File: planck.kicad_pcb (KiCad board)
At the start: 4 copper layers, 38.8 x 39.8 mm, 32 parts, among them J1 USB_C_Receptacle_USB2.0, K1 KEYSW, K2 KEYSW, K3 KEYSW, K4 KEYSW, SW1 SW_PUSH, U1 ATmega32U4-M, Y1 Crystal_GND24_Small

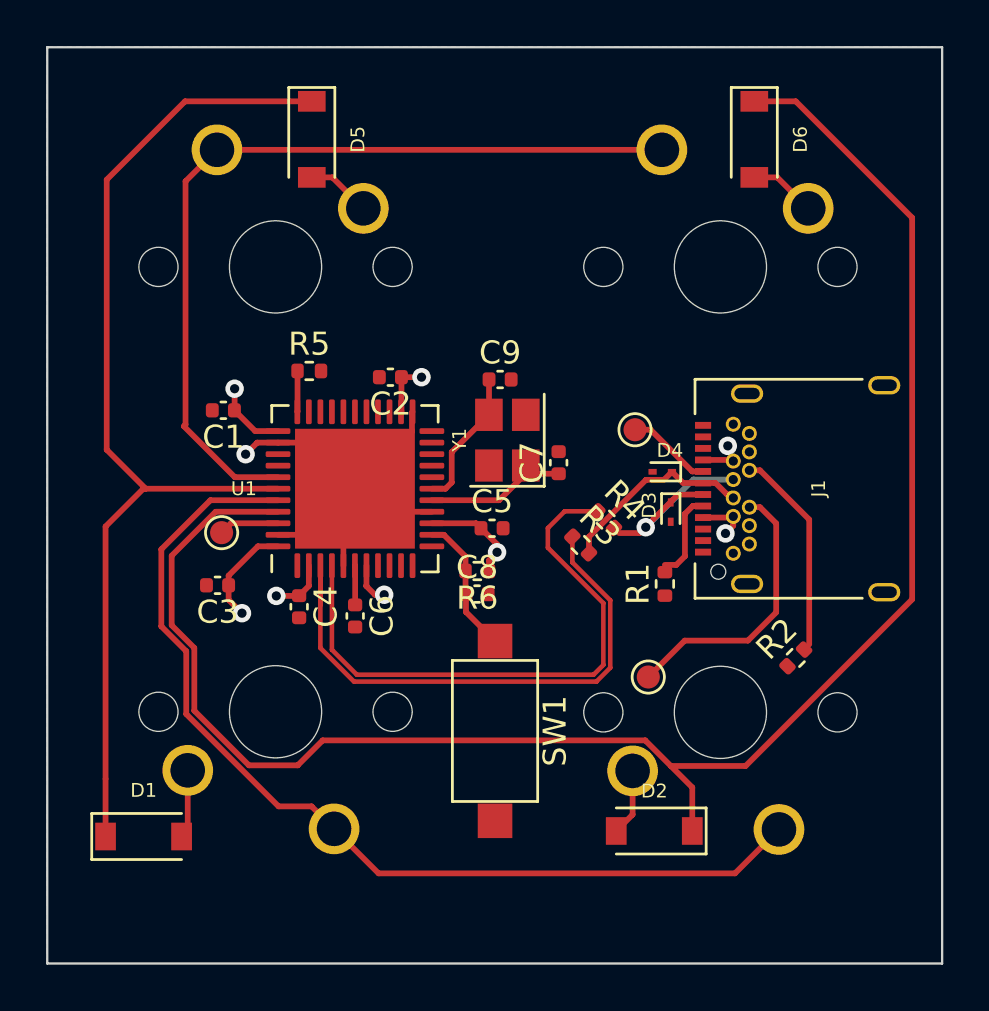
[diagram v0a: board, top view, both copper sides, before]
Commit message: added new usb c
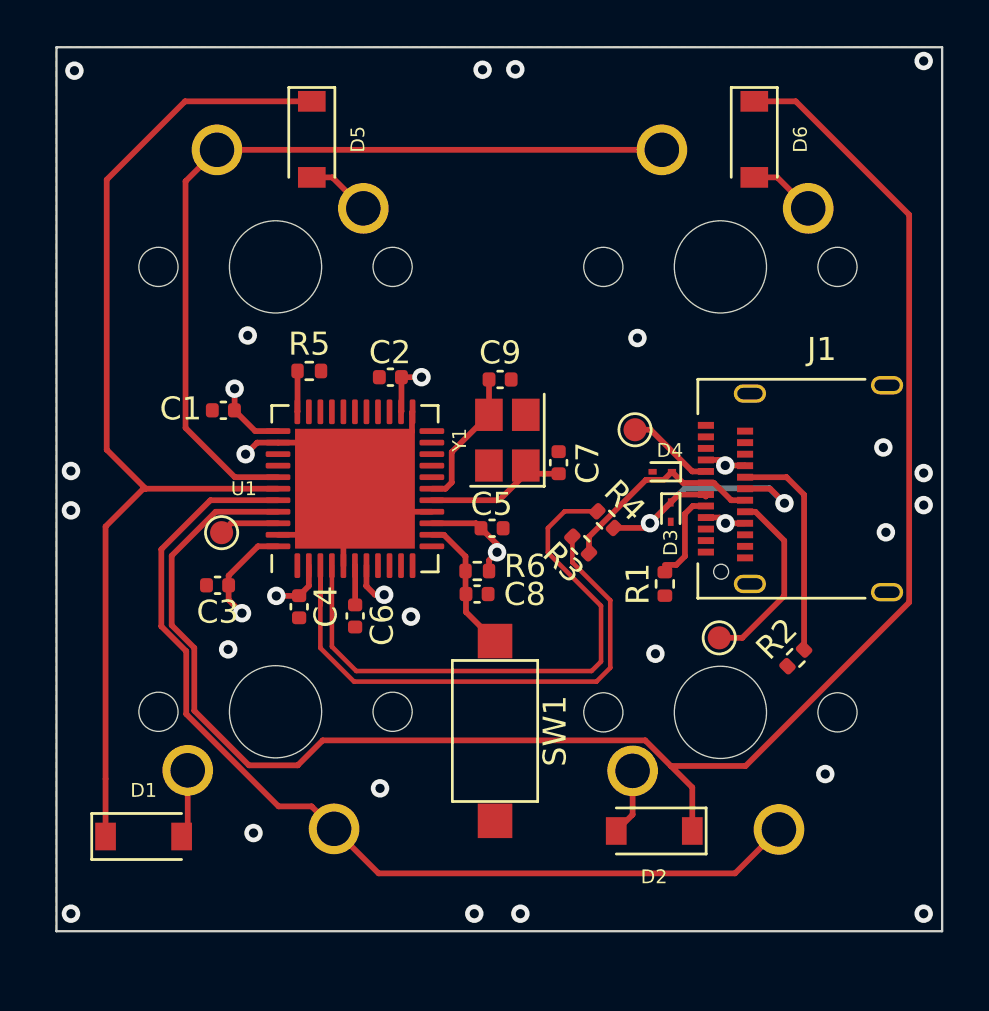
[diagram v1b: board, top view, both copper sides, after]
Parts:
- J1: footprint Connector_USB:USB_C_Receptacle_Amphenol_12401548E4-2A -> Connector_USB:USB_C_Receptacle_Amphenol_12401610E4-2A
- moved TP2 3.52 mm to (106.6, 123.0)
- moved J1 0.12 mm to (111.1, 116.6)
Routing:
- net Net-(D3-Pad1): track 8.99 -> 13.3 mm, vias 1 -> 2
- net Net-(J1-PadB8): track 12.2 -> 8.31 mm
- net Net-(J1-PadB5): track 8.90 -> 9.72 mm
- net Net-(D4-Pad1): track 8.61 -> 9.17 mm
- net GND: vias 1 -> 23
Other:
- board size 38.8 x 39.8 mm -> 38.4 x 38.4 mm
